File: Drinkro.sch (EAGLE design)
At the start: 21 parts, among them J1 POWER_JACKPTH, U1 L293D, U2 L293D

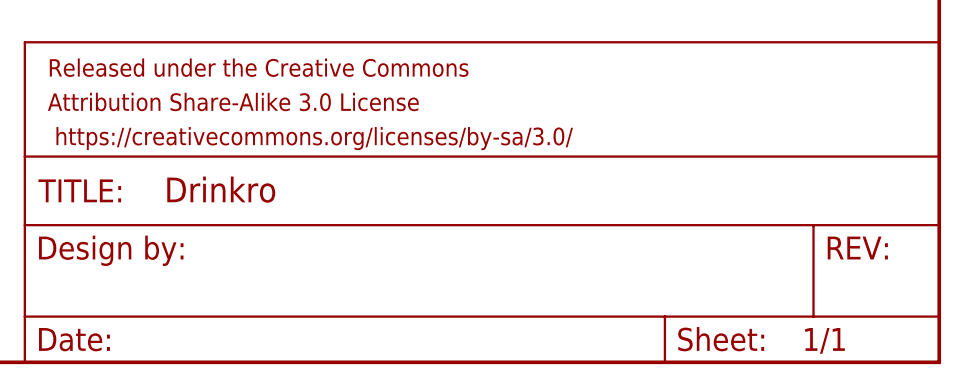
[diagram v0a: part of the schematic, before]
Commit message: Added revision and company.
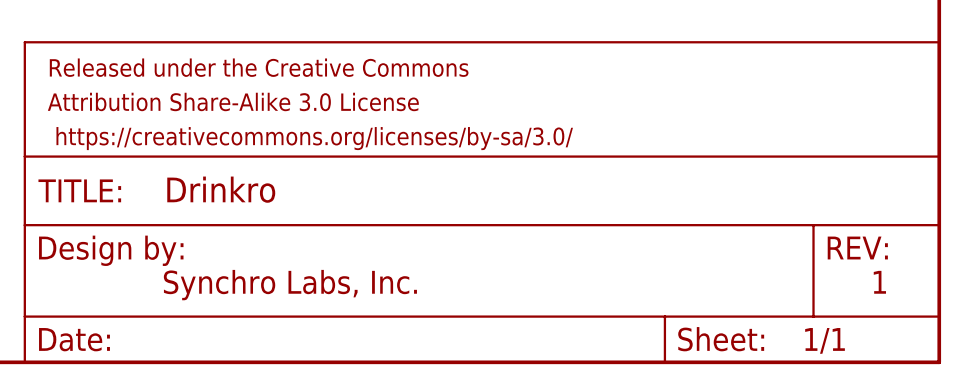
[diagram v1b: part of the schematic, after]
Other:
- note added: "1"
- note added: "Synchro Labs, Inc."
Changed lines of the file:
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@@
 <sheet>
 <plain>
+<text x="162.56" y="7.62" size="2.54" layer="94">Synchro Labs, Inc.</text>
+<text x="241.3" y="7.62" size="2.54" layer="94">1</text>
 </plain>
 <instances>

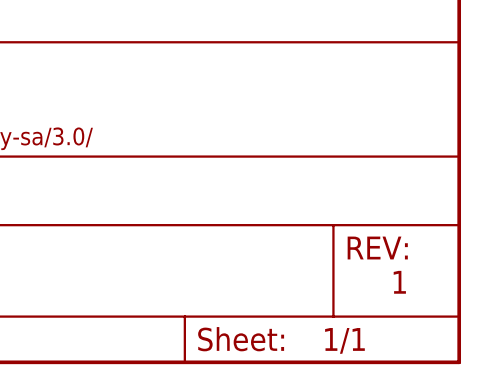
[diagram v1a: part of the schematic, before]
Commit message: Silkscreen changes. Revision bump to 2.
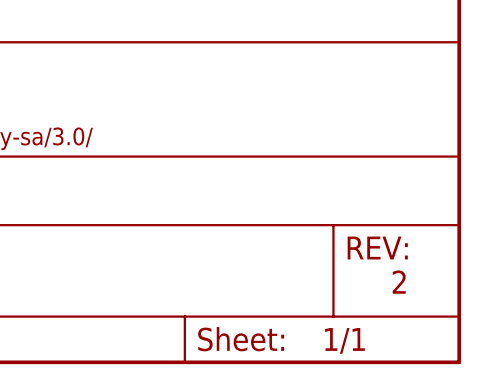
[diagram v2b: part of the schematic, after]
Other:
- note added: "2"
- note removed: "1"
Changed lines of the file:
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@@
 <plain>
 <text x="162.56" y="7.62" size="2.54" layer="94">Synchro Labs, Inc.</text>
-<text x="241.3" y="7.62" size="2.54" layer="94">1</text>
+<text x="241.3" y="7.62" size="2.54" layer="94">2</text>
 </plain>
 <instances>
